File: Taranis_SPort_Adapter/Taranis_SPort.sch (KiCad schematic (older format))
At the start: 12 parts, among them J1 CONN_01X04, J2 CONN_01X05, J3 CONN_01X04, Q1 DMG6602SVT, U1 MCP1754ST-3302E/MB-fixed

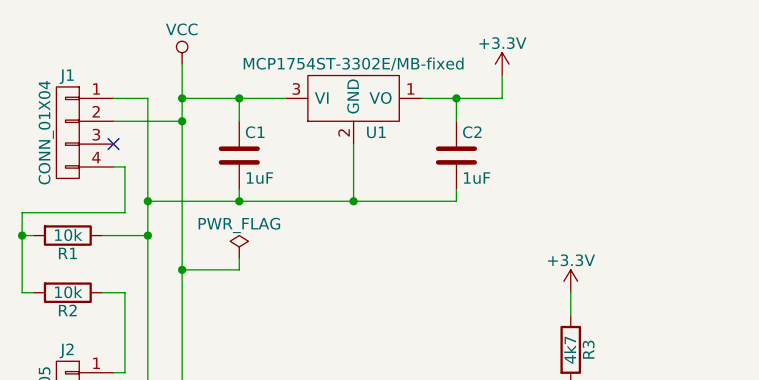
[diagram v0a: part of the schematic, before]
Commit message: Adds a Dual Interter board and Fixes the voltage regulator pin ordering on the SPort adapter board.
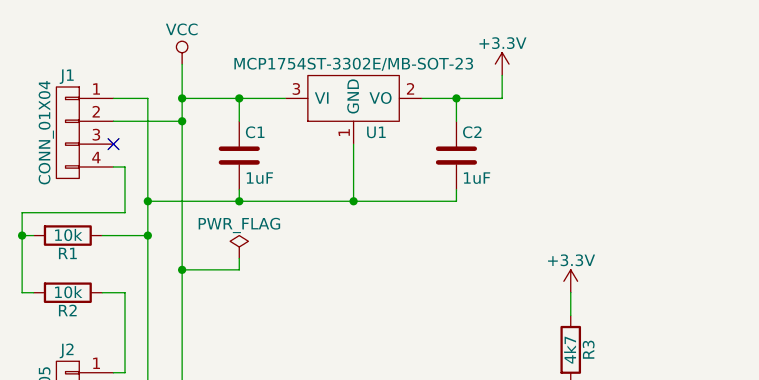
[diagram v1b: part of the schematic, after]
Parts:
- removed U1: MCP1754ST-3302E/MB-fixed, TO_SOT_Packages_SMD:SOT-23_Handsoldering, symbol MCP1754ST-3302E/MB-fixed
- added U1: MCP1754ST-3302E/MB-SOT-23, symbol MCP1754ST-3302E/MB-SOT-23
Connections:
- net +3V3: now also U1.2 (VO)
- net GND: now also U1.1 (GND)
- net VCC: now also U1.3 (VI)
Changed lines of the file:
@@
 LIBS:valves
 LIBS:local
-LIBS:Taranis SPort-cache
+LIBS:Taranis_SPort-cache
 EELAYER 25 0
 EELAYER END
@@
 Copyright 2017 Brian Webb\nReleased under the GNU General Public License V3.0
 $Comp
-L MCP1754ST-3302E/MB-fixed U1
-U 1 1 58F8177D
+L MCP1754ST-3302E/MB-SOT-23 U1
+U 1 1 58FAD359
 P 4500 3200
 F 0 "U1" H 4600 3050 50  0000 C CNN
-F 1 "MCP1754ST-3302E/MB-fixed" H 4500 3350 50  0000 C CNN
-F 2 "TO_SOT_Packages_SMD:SOT-23_Handsoldering" H 4500 3200 50  0001 C CNN
+F 1 "MCP1754ST-3302E/MB-SOT-23" H 4500 3350 50  0000 C CNN
+F 2 "" H 4500 3200 50  0001 C CNN
 F 3 "" H 4500 3200 50  0001 C CNN
 	1    4500 3200

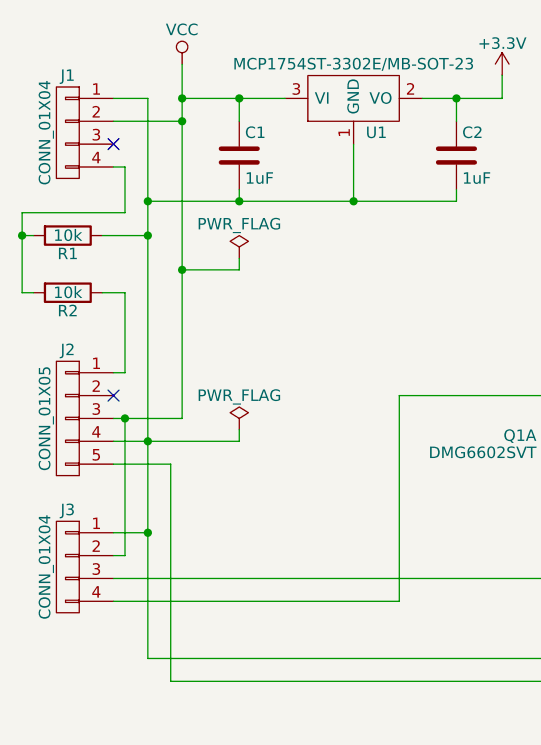
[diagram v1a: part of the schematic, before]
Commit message: Adds S.Port Rx to second (PPM) connector on S.Port Adapter.
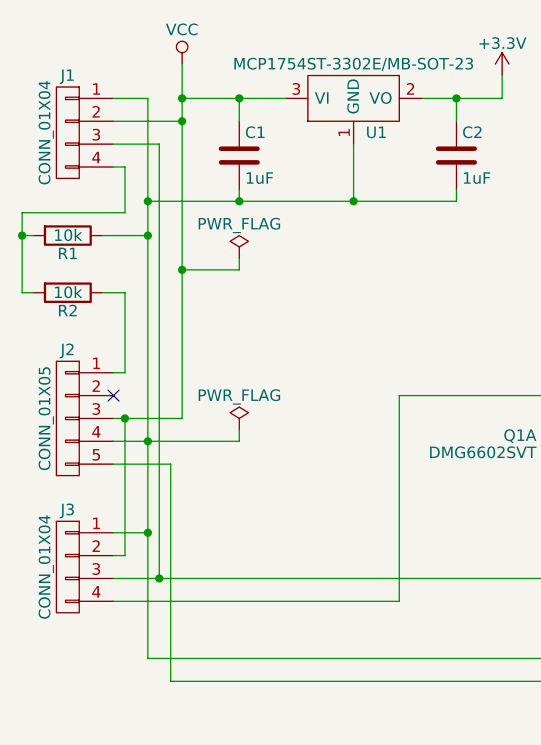
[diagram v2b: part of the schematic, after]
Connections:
- net at J3.3 (P3), Q1.3 (G): now also J1.3 (P3)
- no-connect marks 2 -> 1
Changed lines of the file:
@@
 Wire Wire Line
 	3500 3500 3450 3500
-NoConn ~ 3450 3400
 Text Notes 6450 7150 0    60   ~ 0
 Copyright 2017 Brian Webb\nReleased under the GNU General Public License V3.0
@@
 	1    0    0    -1
 $EndComp
+Wire Wire Line
+	3450 3400 3650 3400
+Wire Wire Line
+	3650 3400 3650 5300
+Connection ~ 3650 5300
 $EndSCHEMATC
